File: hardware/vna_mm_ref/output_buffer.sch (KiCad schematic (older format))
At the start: 22 parts

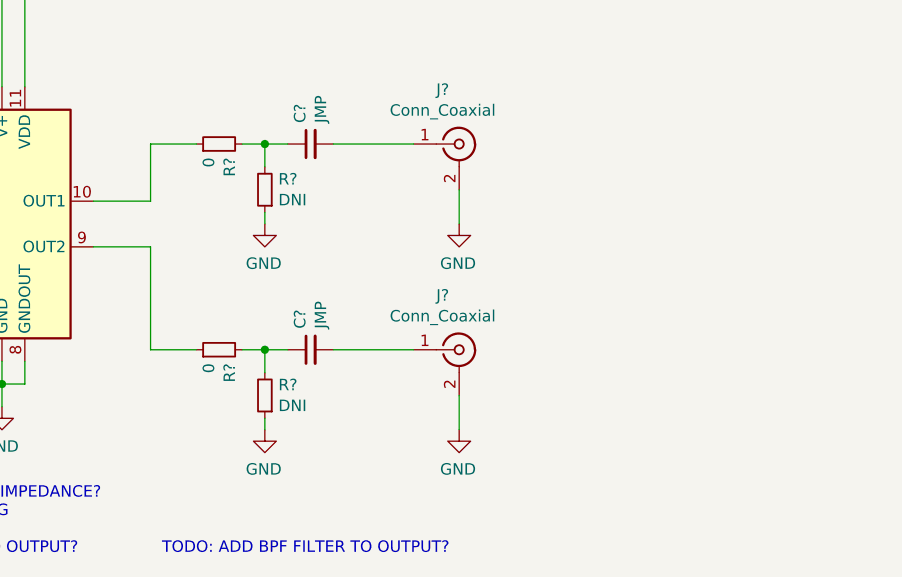
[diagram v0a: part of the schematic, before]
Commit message: added relay for ext ref input
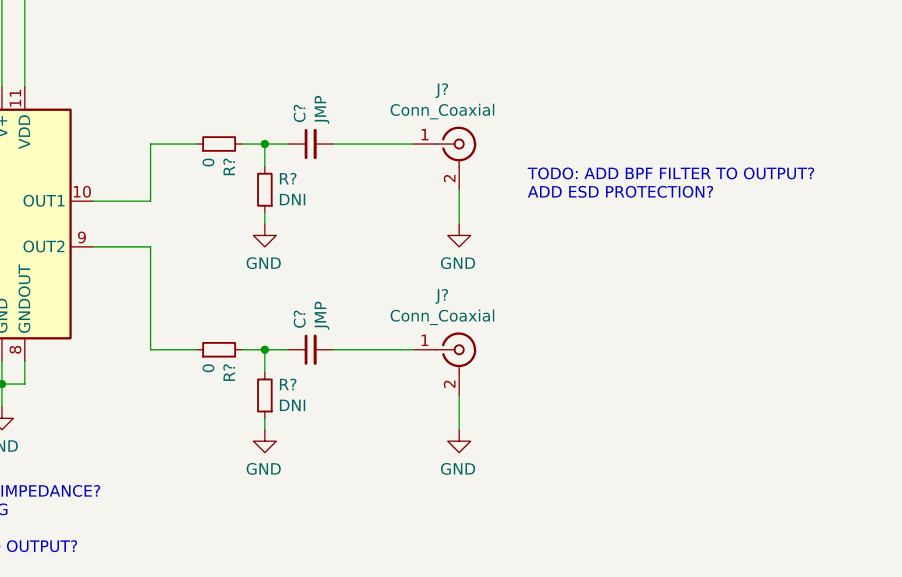
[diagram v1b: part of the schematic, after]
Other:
- note added: "TODO: ADD BPF FILTER TO OUTPUT?\nADD ESD PROTECTION?"
- note removed: "TODO: ADD BPF FILTER TO OUTPUT?"
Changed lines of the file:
@@
 Wire Wire Line
 	6200 4300 6300 4300
-Text Notes 5850 5200 0    50   ~ 0
-TODO: ADD BPF FILTER TO OUTPUT?
+Text Notes 7450 3650 0    50   ~ 0
+TODO: ADD BPF FILTER TO OUTPUT?\nADD ESD PROTECTION?
 Wire Wire Line
 	6950 4300 6600 4300

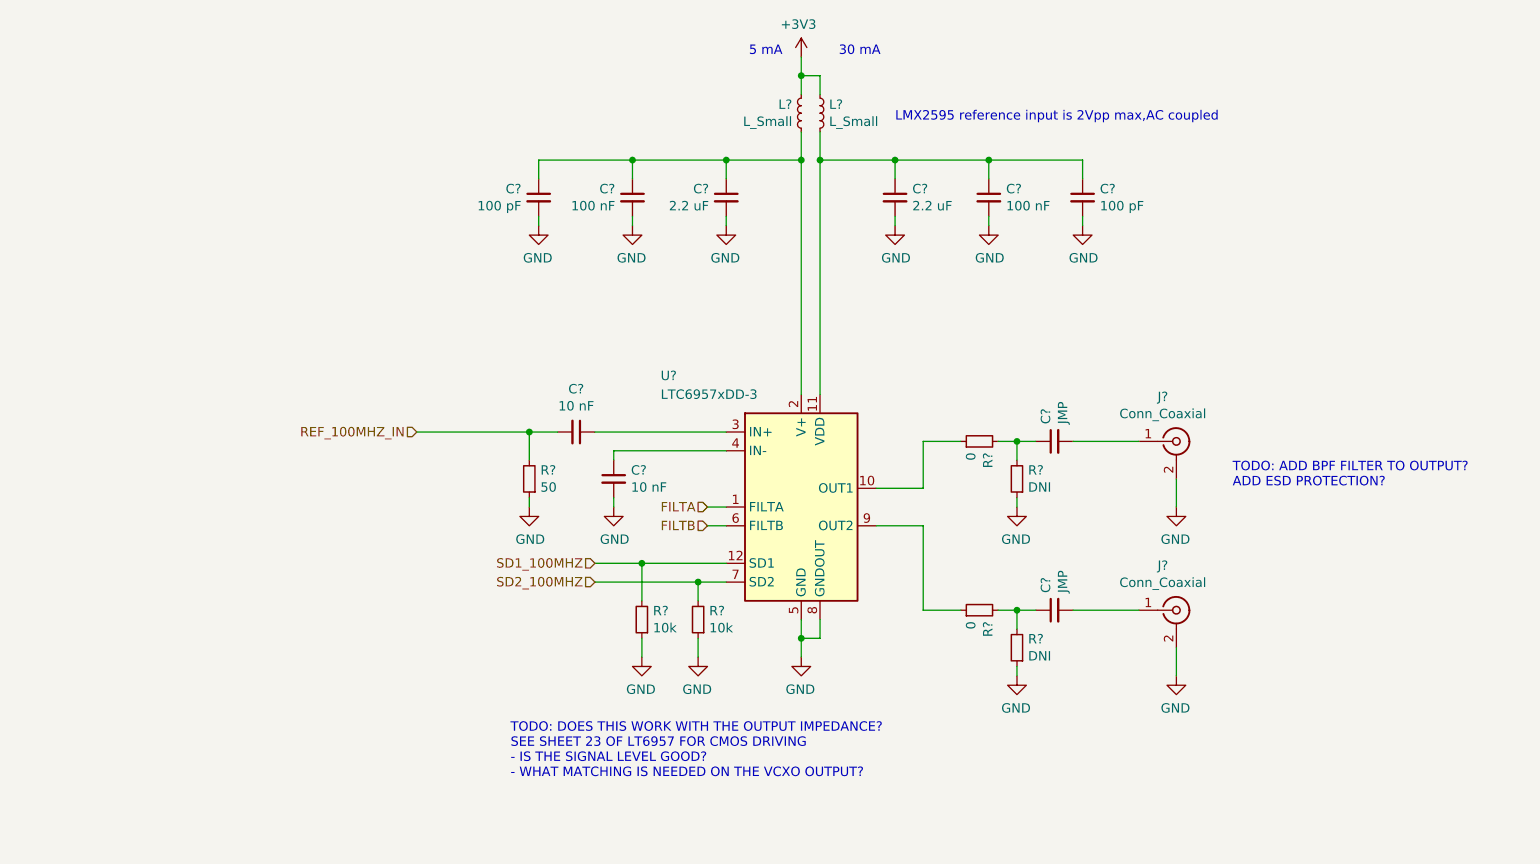
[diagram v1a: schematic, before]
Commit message: added regulator to vna mm ref board
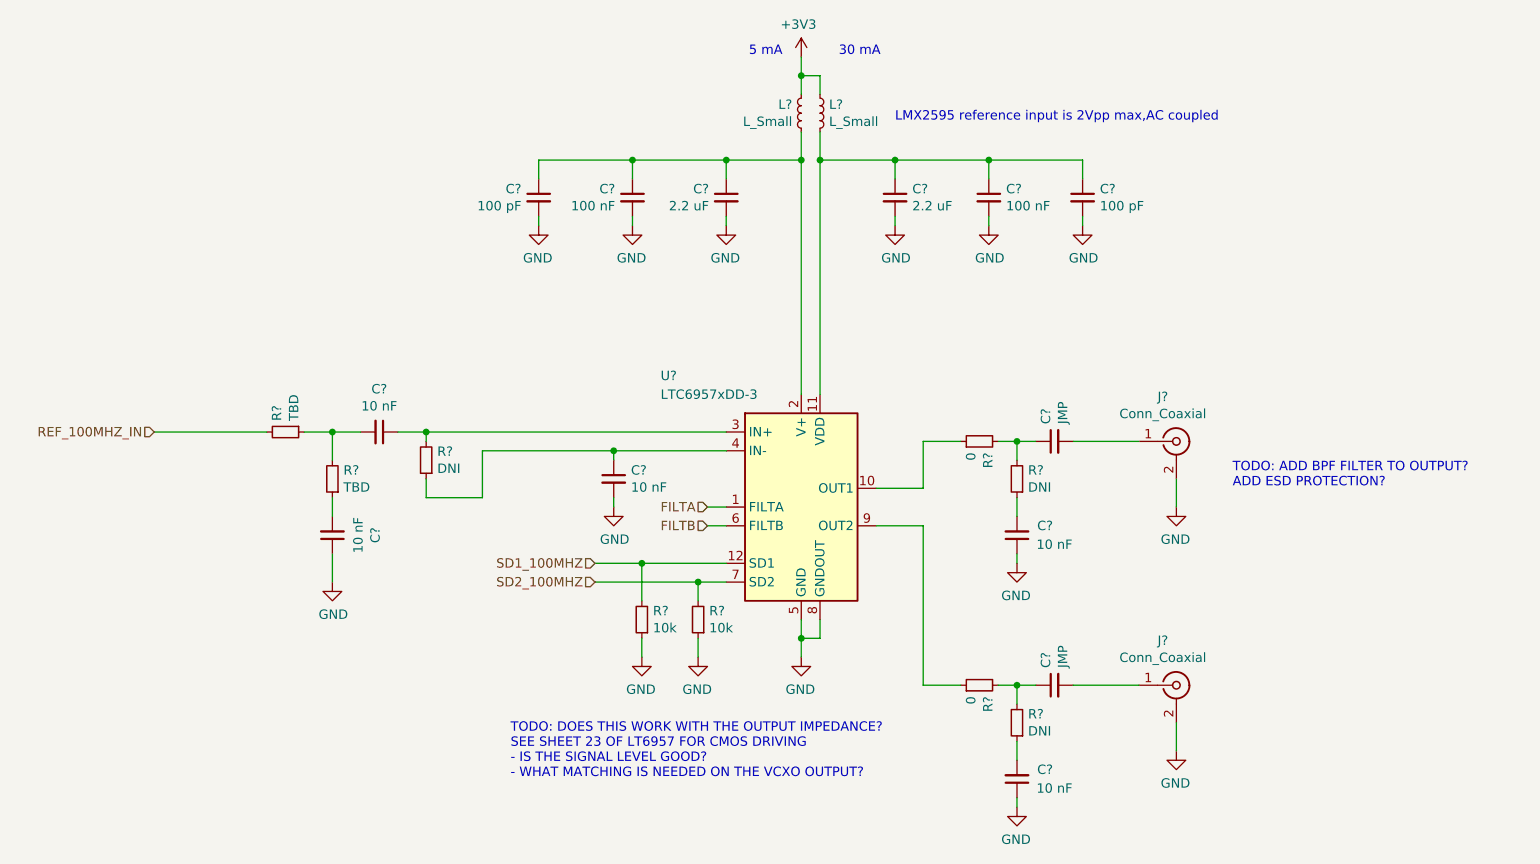
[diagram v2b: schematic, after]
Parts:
- added C? (x3): 10 nF, symbol Device:C_Small
- added R?: TBD, symbol Device:R_Small
- added R?: DNI, symbol Device:R_Small
- R?: value 50 -> TBD
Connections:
- net GND: now also C?.1, C?.1, C?.1; no longer R?.1, R?.1, R?.1
- net REF_100MHZ_IN: now also R?.2; no longer C?.2, R?.2
- net at C?.1, U?.3 (IN+): now also R?.2
- net at C?.1, U?.4 (IN-): now also R?.1
- new net: C?.2, R?.1, R?.2
- new net: C?.2, R?.1 (x3)
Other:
- moved on the sheet: C?, J?, R?

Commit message: added protection to digital inputs
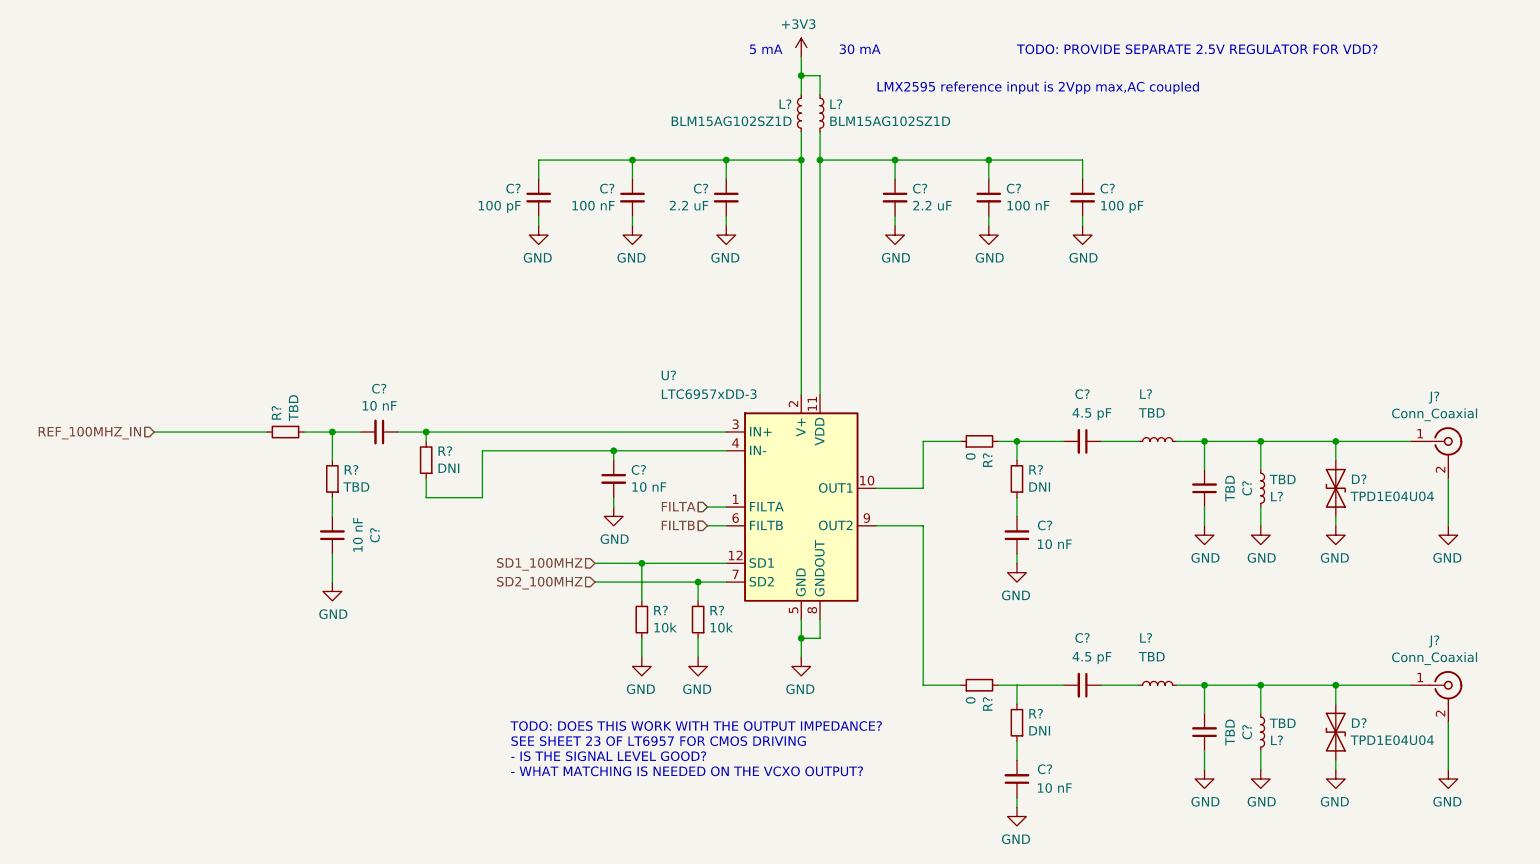
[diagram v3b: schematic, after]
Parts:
- removed C? (x2): JMP, symbol Device:C_Small
- removed J?: Conn_Coaxial, symbol Connector:Conn_Coaxial
- added C? (x2): 4.5 pF, symbol Device:C_Small
- added C? (x2): TBD, symbol Device:C_Small
- added D? (x2): TPD1E04U04, symbol Device:D_TVS
- added J?: Conn_Coaxial, symbol Connector:Conn_Coaxial
- added L? (x4): TBD, symbol Device:L_Small
- L? (x2): value L_Small -> BLM15AG102SZ1D
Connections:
- net GND: now also C?.1, C?.1, D?.2 (A2), D?.2 (A2), J?.2 (Ext), L?.1, L?.1
- net at R?.2, R?.2: now also C?.2 (x2)
- net at J?.1 (In): now also C?.2, D?.1 (A1), L?.1, L?.2
- new net: C?.1, L?.2 (x2)
- new net: C?.2, D?.1 (A1), J?.1 (In), L?.1, L?.2
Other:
- note added: "TODO: PROVIDE SEPARATE 2.5V REGULATOR FOR VDD?"
- note removed: "TODO: ADD BPF FILTER TO OUTPUT?\nADD ESD PROTECTION?"
- moved on the sheet: J?

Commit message: footprint assignment on reference board
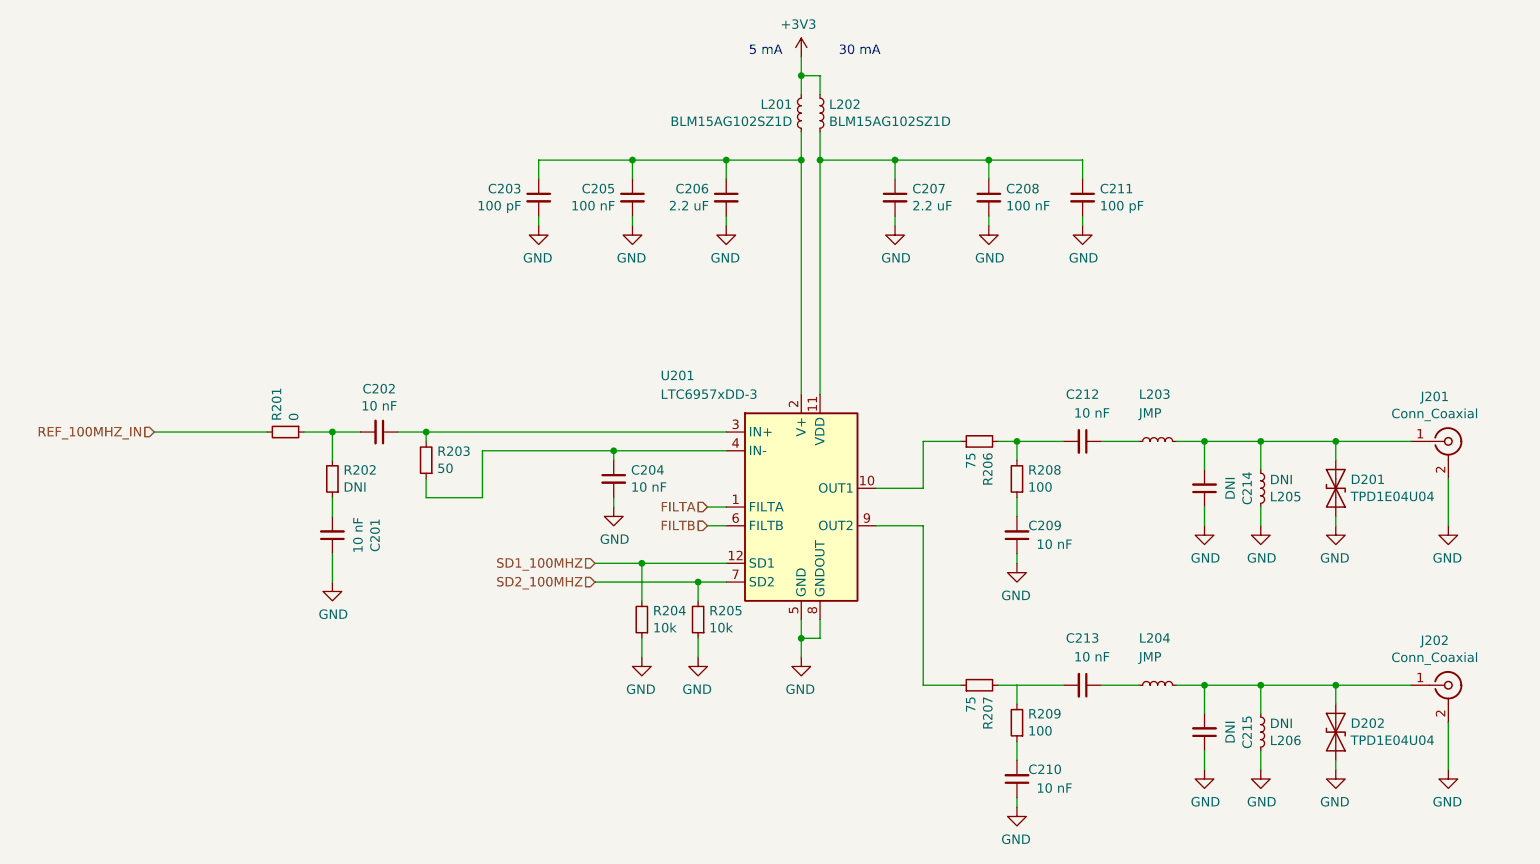
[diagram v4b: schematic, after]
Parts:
- C201, C202, C203, C204, C205, C208, C209, C210, C211: renamed from C?; footprint (none) -> Capacitor_SMD:C_0402_1005Metric
- C206, C207: renamed from C?; footprint (none) -> Capacitor_SMD:C_0603_1608Metric
- C212, C213: renamed from C?; value 4.5 pF -> 10 nF; footprint (none) -> Capacitor_SMD:C_0402_1005Metric
- C214, C215: renamed from C?; value TBD -> DNI; footprint (none) -> Capacitor_SMD:C_0402_1005Metric
- D201, D202: renamed from D?; footprint (none) -> Diode_SMD:D_0402_1005Metric
- J201, J202: renamed from J?; footprint (none) -> Connector_Coaxial:SMA_Amphenol_132289_EdgeMount
- L201, L202: renamed from L?; footprint (none) -> Inductor_SMD:L_0402_1005Metric
- L203, L204: renamed from L?; value TBD -> JMP; footprint (none) -> Inductor_SMD:L_0805_2012Metric
- L205, L206: renamed from L?; value TBD -> DNI; footprint (none) -> Inductor_SMD:L_0402_1005Metric
- R201: renamed from R?; value TBD -> 0; footprint (none) -> Resistor_SMD:R_0402_1005Metric
- R202: renamed from R?; value TBD -> DNI; footprint (none) -> Resistor_SMD:R_0402_1005Metric
- R203: renamed from R?; value DNI -> 50; footprint (none) -> Resistor_SMD:R_0402_1005Metric
- R204, R205: renamed from R?; footprint (none) -> Resistor_SMD:R_0402_1005Metric
- R206, R207: renamed from R?; value 0 -> 75; footprint (none) -> Resistor_SMD:R_0402_1005Metric
- R208, R209: renamed from R?; value DNI -> 100; footprint (none) -> Resistor_SMD:R_0402_1005Metric
- gave numbers to parts that had none: 1
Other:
- note removed: "LMX2595 reference input is 2Vpp max,AC coupled"
- note removed: "TODO: DOES THIS WORK WITH THE OUTPUT IMPEDANCE?\nSEE SHEET 23 OF LT6957 FOR CMOS DRIVING\n- IS THE SIGNAL LEVEL GOOD?\n- WHAT MATCHING IS NEEDED ON THE VCXO OUTPUT?"
- note removed: "TODO: PROVIDE SEPARATE 2.5V REGULATOR FOR VDD?"
